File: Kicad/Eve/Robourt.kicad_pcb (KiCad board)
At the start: 4 copper layers, 141.8 x 126 mm, 122 parts, among them IC1 STM32U535RET6, J1 Conn_ST_STDC14, J10 Conn_01x04, J2 Conn_01x02, J3 Conn_02x20_Odd_Even, J4 Conn_01x03, J5 Conn_01x03, J8 Conn_01x04, J9 Conn_01x04, Q1 SQJ504EP-T1_GE3, Q10 SQJ504EP-T1_GE3, Q11 SQJ504EP-T1_GE3, Q12 SQJ504EP-T1_GE3, Q2 SQJ504EP-T1_GE3, Q3 SQJ504EP-T1_GE3, Q4 SQJ504EP-T1_GE3, Q5 SQJ504EP-T1_GE3, Q6 SQJ504EP-T1_GE3, Q7 SQJ504EP-T1_GE3, Q8 SQJ504EP-T1_GE3, Q9 SQJ504EP-T1_GE3, SW2 SW_Push, U1 BU33SD5WG-TR, U3 TMC2590-TA, U4 TMC2590-TA, U5 TMC2590-TA, Y2 Crystal

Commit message: pulled last changes from charlotte
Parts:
- moved R4 9.03 mm to (122.7, 121.2)
- moved C7 9.03 mm to (119.7, 124.8)
- moved D3 9.03 mm to (125.0, 121.2)
- moved U1 9.03 mm to (123.7, 125.9)
- moved C6 9.03 mm to (119.7, 127.0)
- moved R20 2.36 mm to (81.2, 129.8)
- moved R23 1.60 mm to (93.8, 133.9)
- moved R28 1.32 mm to (69.7, 90.3)
- moved R22 1.31 mm to (83.0, 133.9)
- moved C21 0.81 mm to (87.9, 118.5)
- moved R8 0.74 mm to (95.0, 128.2)
- moved R31 0.64 mm to (81.0, 94.3)
- moved C47 0.51 mm to (75.8, 80.4)
- moved R30 0.37 mm to (71.6, 94.2)
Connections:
- U4 pad 26: /driver_stepper1/STANDALONE_MODE -> (no net)
- U4 pad 27: /driver_stepper1/SG_TST -> (no net)
- U5 pad 26: /driver_stepper2/STANDALONE_MODE -> (no net)
- U5 pad 27: /driver_stepper2/SG_TST -> (no net)
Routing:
- net SPI2_MISO: track 0.00 -> 106.4 mm, vias 0 -> 3
- net SPI2_MOSI: track 0.00 -> 106.4 mm, vias 0 -> 3
- net /driver_stepper2/B1: track 2.23 -> 77.9 mm, vias 0 -> 2
- net /driver_stepper2/B2: track 2.23 -> 75.6 mm, vias 0 -> 2
- net GPIO_STEP3: track 0.00 -> 61.1 mm, vias 0 -> 2
- net /driver_stepper/B1: track 2.23 -> 62.0 mm
- net GPIO_DIR3: track 0.00 -> 59.2 mm, vias 0 -> 2
- net 24V: track 0.00 -> 58.0 mm, vias 0 -> 14
- net GPIO_CSN3: track 0.00 -> 53.7 mm, vias 0 -> 2
- net /driver_stepper/B2: track 2.23 -> 55.2 mm
- net /driver_stepper2/5VOUT: track 0.00 -> 50.0 mm, vias 0 -> 2
- net SCK: track 0.00 -> 48.2 mm, vias 0 -> 2
- net /driver_stepper2/VHS: track 0.00 -> 47.6 mm, vias 0 -> 2
- net UART4_TX: track 0.00 -> 37.6 mm, vias 0 -> 2
- net /driver_stepper/5VOUT: track 0.00 -> 37.4 mm, vias 0 -> 2
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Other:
- board text added: "EVE"

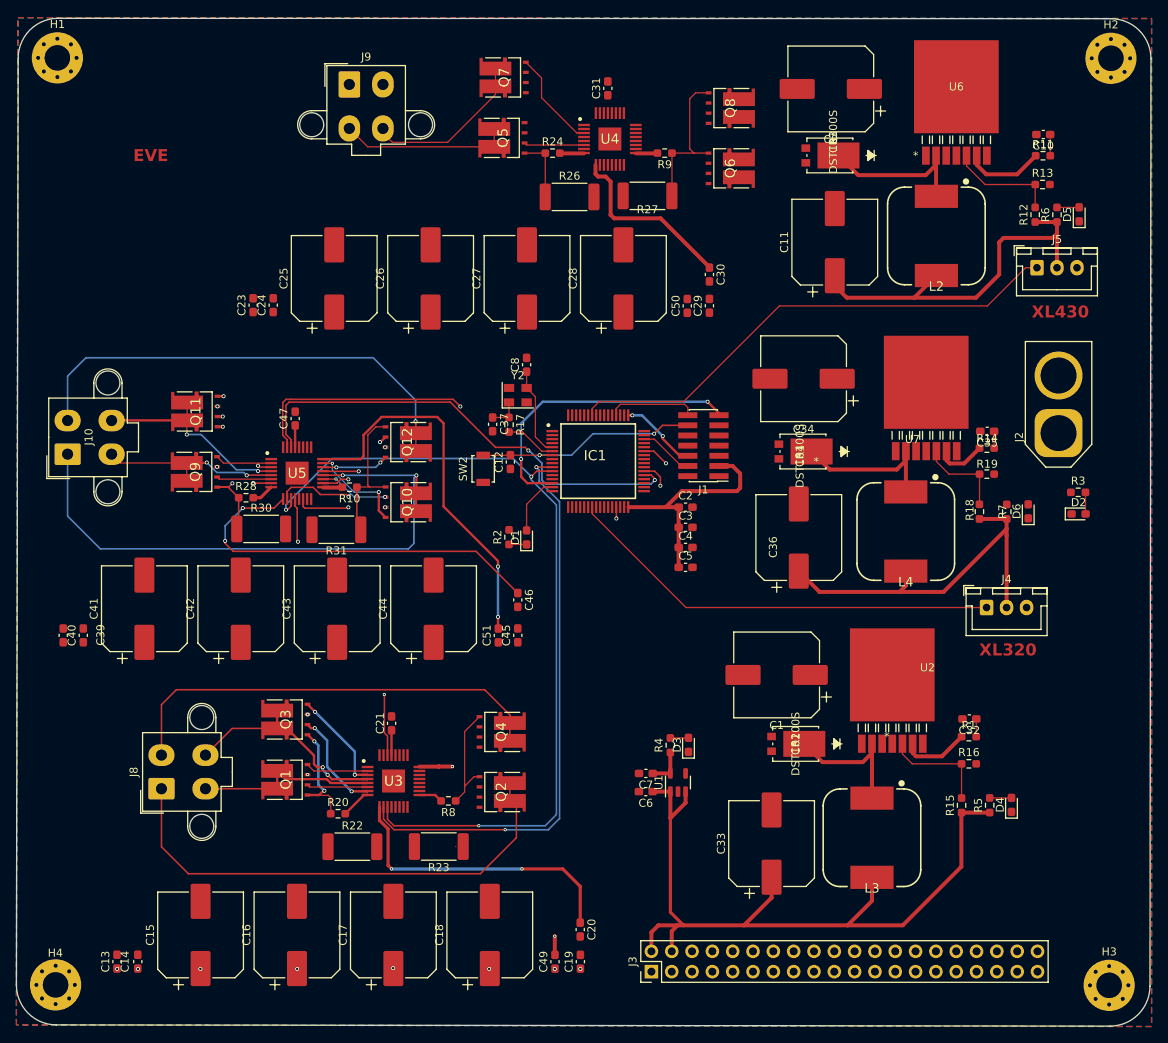
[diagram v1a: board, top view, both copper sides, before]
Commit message: finished routing errors remain
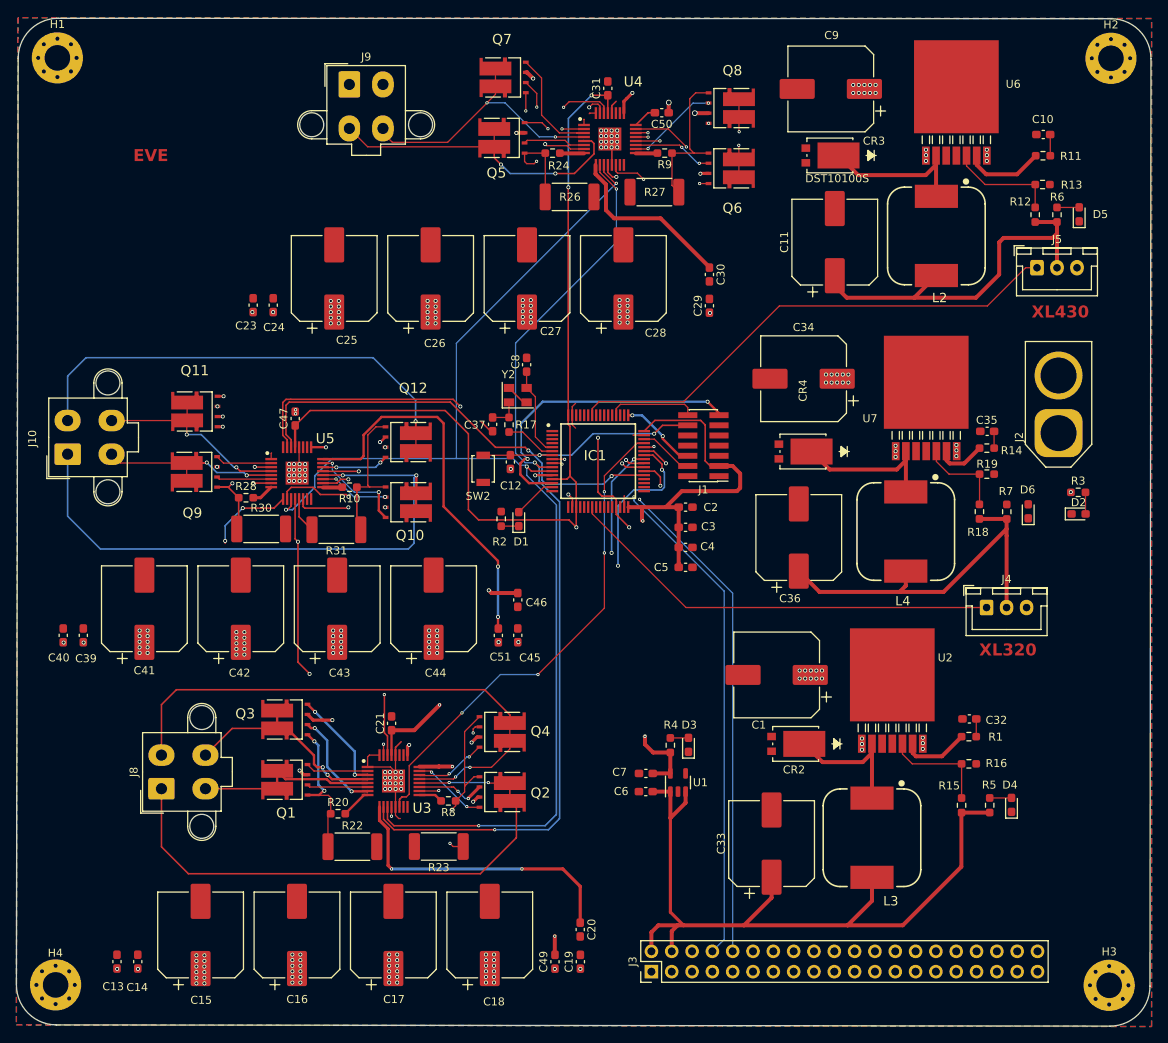
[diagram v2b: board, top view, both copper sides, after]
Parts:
- moved C50 24.4 mm to (121.7, 42.2), turned to 180 degrees
- moved D1 2.49 mm to (103.8, 93.0)
- moved R2 2.49 mm to (101.6, 92.9)
- moved R27 0.98 mm to (120.8, 52.1)
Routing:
- net +3.3V: track 39.6 -> 242.4 mm, vias 0 -> 6
- net SCK: track 48.2 -> 137.6 mm, vias 2 -> 6
- net LPUART1_TX: track 0.00 -> 75.9 mm, vias 0 -> 2
- net LPUART1_RX: track 0.00 -> 74.9 mm, vias 0 -> 2
- net GPIO_CSN1: track 0.00 -> 61.7 mm, vias 0 -> 4
- net GPIO_STEP1: track 0.00 -> 60.0 mm, vias 0 -> 3
- net GPIO_DIR2: track 0.00 -> 59.5 mm, vias 0 -> 2
- net /driver_stepper1/B1: track 0.00 -> 58.9 mm, vias 0 -> 2
- net /driver_stepper1/B2: track 0.00 -> 54.7 mm, vias 0 -> 2
- net GPIO_STEP2: track 0.00 -> 52.7 mm, vias 0 -> 2
- net GPIO_DIR1: track 7.73 -> 57.6 mm, vias 1 -> 3
- net SPI2_MOSI: track 106.4 -> 153.5 mm, vias 3 -> 4
- net SPI2_MISO: track 106.4 -> 152.8 mm, vias 3 -> 4
- net GND: track 0.00 -> 44.3 mm, vias 0 -> 53
- net GPIO_CSN2: track 0.00 -> 39.9 mm, vias 0 -> 2
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
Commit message: started cleaning PCB
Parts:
- moved C14 73.4 mm to (119.4, 111.0)
- moved C13 73.4 mm to (116.8, 111.0)
- moved C39 58.7 mm to (105.6, 107.1)
- moved C40 58.7 mm to (108.1, 107.1)
- moved Q3 14.2 mm to (62.7, 120.1)
- moved Q1 14.1 mm to (62.7, 127.4)
- moved J8 13.0 mm to (46.1, 127.2)
- moved R22 10.1 mm to (73.1, 131.7)
- moved Q4 9.55 mm to (109.1, 118.7), turned to 90 degrees
- moved C15 6.88 mm to (57.1, 145.2)
- moved C16 6.88 mm to (69.2, 145.2)
- moved C17 6.88 mm to (81.2, 145.2)
- moved C18 6.88 mm to (93.3, 145.2)
- moved R8 1.51 mm to (94.8, 129.7)
- moved C42 0.15 mm to (69.2, 104.2)
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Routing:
- net /driver_stepper/B2: track 69.1 -> 6.79 mm
- net /driver_stepper/B1: track 73.4 -> 13.6 mm
- net /driver_stepper/A1: track 23.1 -> 0.00 mm
- net /driver_stepper/A2: track 27.4 -> 10.8 mm, vias 2 -> 1
- net Net-(Q1-S1): track 18.2 -> 10.4 mm, vias 2 -> 0
- net 24V: track 19.4 -> 13.4 mm, vias 204 -> 201
- net /driver_stepper/HA1: track 7.85 -> 2.20 mm
- net /driver_stepper/HB1: track 9.39 -> 13.7 mm
- net /driver_stepper/LB2: track 12.9 -> 16.7 mm, vias 2 -> 3
- net GPIO_DIR1: track 57.6 -> 54.4 mm
- net /driver_stepper/SRB: track 3.02 -> 4.48 mm
- net /driver_stepper/HA2: track 12.9 -> 11.4 mm, vias 2 -> 1
- net GND: track 44.3 -> 42.9 mm
- net +3.3V: track 242.4 -> 241.3 mm
- net Net-(Q2-S1): track 21.7 -> 22.4 mm, vias 2 -> 1
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
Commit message: EVE 2.0 WIP
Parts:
- removed C15, C16, C17, C18, C25, C26: 150u, Capacitor_SMD:CP_Elec_10x10.5
- moved J2 117.2 mm to (74.4, 148.2), turned to 180 degrees
- moved C13 77.6 mm to (72.0, 47.5), turned to 180 degrees
- moved Q6 66.7 mm to (61.8, 55.4), turned to 90 degrees
- moved Q8 63.0 mm to (68.5, 61.8), turned to 180 degrees
- moved C30 61.9 mm to (65.8, 58.1), turned to 180 degrees
- moved C41 56.8 mm to (87.6, 56.2), turned to 0 degrees
- moved Reset 56.5 mm to (123.8, 35.8)
- moved C12 56.0 mm to (128.3, 36.0)
- moved C14 53.2 mm to (75.6, 80.8), turned to 0 degrees
- moved J1 50.8 mm to (109.9, 35.9), turned to -90 degrees
- moved R9 48.8 mm to (75.0, 60.4), turned to 0 degrees
- moved C45 47.5 mm to (87.9, 62.8), turned to 0 degrees
- moved R2 46.6 mm to (121.0, 50.5), turned to -90 degrees
- moved D1 46.5 mm to (122.8, 50.5), turned to -90 degrees
- moved C20 45.4 mm to (68.5, 129.7), turned to 180 degrees
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- renumbered SW2 to Reset
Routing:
- net 5.1V: track 96.8 -> 37.5 mm, vias 0 -> 47
- net /driver_stepper/B2: track 6.79 -> 64.9 mm
- net GND: track 42.9 -> 99.0 mm
- net UART4_RX: track 11.1 -> 66.0 mm, vias 0 -> 2
- net /NRST: track 28.7 -> 79.2 mm
- net /SYS_JTMS-SWDIO: track 6.85 -> 55.5 mm, vias 0 -> 2
- net /SYS_JTMS-SWCLK: track 9.75 -> 58.0 mm
- net /driver_stepper2/5VOUT: track 49.8 -> 4.20 mm, vias 3 -> 0
- net /driver_stepper2/VHS: track 47.6 -> 4.47 mm, vias 2 -> 0
- net 7.5V: track 47.7 -> 4.94 mm, vias 0 -> 47
- net +3.3V: track 241.3 -> 281.9 mm, vias 6 -> 12
- net /driver_stepper/B1: track 13.6 -> 52.0 mm
- net /driver_stepper2/B1: track 77.8 -> 43.8 mm
- net /driver_stepper/5VOUT: track 37.4 -> 5.12 mm, vias 2 -> 0
- net /driver_stepper/VHS: track 33.6 -> 2.90 mm, vias 2 -> 0
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- added copper zone on In2.Cu, net +3.3V
- added copper zone on In2.Cu, net 5.1V
- added copper zone on In2.Cu, net 7.5V

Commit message: update pcb
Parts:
- removed C12, C13, C14, C19, C21, C23, C24, C29, C31, C39, C40, C45, C47: 100n, Capacitor_SMD:C_0603_1608Metric_Pad1.08x0.95mm_HandSolder
- removed C20, C30, C46: 470n, Capacitor_SMD:C_0603_1608Metric_Pad1.08x0.95mm_HandSolder
- removed C27, C28, C41, C42, C43, C44: 150u, Capacitor_SMD:CP_Elec_10x10.5
- removed C37, C8: 10p, Capacitor_SMD:C_0603_1608Metric_Pad1.08x0.95mm_HandSolder
- removed C49, C50, C51: 220n, Capacitor_SMD:C_0603_1608Metric_Pad1.08x0.95mm_HandSolder
- removed C6, C7: 1u, Capacitor_SMD:C_0603_1608Metric_Pad1.08x0.95mm_HandSolder
- removed D3: LED, LED_SMD:LED_0603_1608Metric_Pad1.05x0.95mm_HandSolder
- removed J10, J8, J9: Conn_01x04, Connector_Molex:Molex_Mini-Fit_Jr_5566-04A2_2x02_P4.20mm_Vertical
- removed Q1, Q10, Q11, Q12, Q2, Q3, Q4, Q5, Q6, Q7, Q8, Q9: SQJ504EP-T1_GE3, Mosfet:SQJ968EPT1GE3
- removed R10, R20, R24, R28, R8, R9: 10, Resistor_SMD:R_0603_1608Metric_Pad0.98x0.95mm_HandSolder
- removed R17: 10R, Resistor_SMD:R_0603_1608Metric_Pad0.98x0.95mm_HandSolder
- removed R22, R23, R26, R27, R30, R31: 0.075, Resistor_SMD:R_2512_6332Metric_Pad1.40x3.35mm_HandSolder
- removed R4: 1k, Resistor_SMD:R_0603_1608Metric_Pad0.98x0.95mm_HandSolder
- removed Reset: SW_Push, Button_Switch_SMD:SW_SPST_B3U-1000P
- removed U1: BU33SD5WG-TR, Package_TO_SOT_SMD:SOT-23-5
- removed U3, U4, U5: TMC2590-TA, TMC2590:QFP50P700X700X114-33N
- removed Y2: Crystal, Crystal:Crystal_SMD_EuroQuartz_MT-4Pin_3.2x2.5mm
- added C103: 100n, Capacitor_SMD:C_0402_1005Metric, F.Cu at (307.2, -139.6)
- added C104: 100n, Capacitor_SMD:C_0402_1005Metric, F.Cu at (307.2, -137.6)
- added C107: 100n, Capacitor_SMD:C_0402_1005Metric, F.Cu at (377.5, -135.3)
- added C108: 100n, Capacitor_SMD:C_0402_1005Metric, F.Cu at (377.5, -130.3)
- added C109: 100n, Capacitor_SMD:C_0402_1005Metric, F.Cu at (307.2, -135.7)
- added C110: 100n, Capacitor_SMD:C_0402_1005Metric, F.Cu at (307.2, -133.7)
- added C111: 4.7u, Capacitor_SMD:C_0402_1005Metric, F.Cu at (377.5, -132.8)
- added C112: 100n, Capacitor_SMD:C_0402_1005Metric, F.Cu at (13.2, -114.3)
- added C113: 100n, Capacitor_SMD:C_0402_1005Metric, F.Cu at (13.2, -112.3)
- added C114: 100n, Capacitor_SMD:C_0402_1005Metric, F.Cu at (13.2, -110.4)
- added C115: 100n, Capacitor_SMD:C_0402_1005Metric, F.Cu at (13.2, -108.4)
- added C116: 10p, Capacitor_SMD:C_0402_1005Metric, F.Cu at (45.0, -25.0)
- added C117: 10p, Capacitor_SMD:C_0402_1005Metric, F.Cu at (45.0, -22.5)
- added C118: 100n, Capacitor_SMD:C_0402_1005Metric, F.Cu at (16.1, -114.3)
- added C119: 100n, Capacitor_SMD:C_0402_1005Metric, F.Cu at (16.1, -112.3)
- added C120: 100n, Capacitor_SMD:C_0402_1005Metric, F.Cu at (16.1, -110.4)
- added C121: 100n, Capacitor_SMD:C_0402_1005Metric, F.Cu at (16.1, -108.4)
- added C201: 100n, Capacitor_SMD:C_0402_1005Metric, F.Cu at (-12.3, -36.1)
- added C202: 100n, Capacitor_SMD:C_0402_1005Metric, F.Cu at (-12.3, -37.1)
- added C203: 10u, Capacitor_SMD:C_2220_5750Metric, B.Cu at (-9.61, -29.9)
- added C204: 150u, Capacitor_SMD:CP_Elec_10x10.5, F.Cu at (-9.61, -43.3)
- added C205: 150u, Capacitor_SMD:CP_Elec_10x10.5, F.Cu at (-9.61, -29.9)
- added C206: 220n, Capacitor_SMD:C_0402_1005Metric, F.Cu at (3.57, -41.7)
- added C207: 100n, Capacitor_SMD:C_0402_1005Metric, F.Cu at (3.27, -38.1)
- added C208: 470n, Capacitor_SMD:C_0402_1005Metric, F.Cu at (3.27, -35.6)
- added C209: 100n, Capacitor_SMD:C_0402_1005Metric, F.Cu at (3.27, -33.1)
- added C301: 100n, Capacitor_SMD:C_0402_1005Metric, F.Cu at (-106.0, 4.65)
- added C302: 100n, Capacitor_SMD:C_0402_1005Metric, F.Cu at (-106.0, 6.62)
- added C303: 10u, Capacitor_SMD:C_2220_5750Metric, F.Cu at (-100.3, 7.14)
- added C304: 150u, Capacitor_SMD:CP_Elec_10x10.5, F.Cu at (-126.3, 9.69)
- added C305: 150u, Capacitor_SMD:CP_Elec_10x10.5, F.Cu at (-126.3, 21.7)
- added C306: 220n, Capacitor_SMD:C_0402_1005Metric, F.Cu at (-106.0, 8.59)
- added C307: 100n, Capacitor_SMD:C_0402_1005Metric, F.Cu at (-106.0, 10.6)
- added C308: 470n, Capacitor_SMD:C_0402_1005Metric, F.Cu at (-106.0, 12.5)
- added C309: 100n, Capacitor_SMD:C_0402_1005Metric, F.Cu at (-106.0, 14.5)
- added C401: 100n, Capacitor_SMD:C_0402_1005Metric, F.Cu at (-129.6, 78.8)
- added C402: 100n, Capacitor_SMD:C_0402_1005Metric, F.Cu at (-129.6, 80.8)
- added C403: 10u, Capacitor_SMD:C_2220_5750Metric, F.Cu at (-123.9, 81.3)
- added C404: 150u, Capacitor_SMD:CP_Elec_10x10.5, F.Cu at (-149.9, 83.8)
- added C405: 150u, Capacitor_SMD:CP_Elec_10x10.5, F.Cu at (-149.9, 95.9)
- added C406: 220n, Capacitor_SMD:C_0402_1005Metric, F.Cu at (-129.6, 82.7)
- added C407: 100n, Capacitor_SMD:C_0402_1005Metric, F.Cu at (-129.6, 84.7)
- added C408: 470n, Capacitor_SMD:C_0402_1005Metric, F.Cu at (-129.6, 86.7)
- added C409: 100n, Capacitor_SMD:C_0402_1005Metric, F.Cu at (-129.6, 88.6)
- added C501: 1u, Capacitor_SMD:C_0402_1005Metric, F.Cu at (229.1, 109.2)
- added C502: 1u, Capacitor_SMD:C_0402_1005Metric, F.Cu at (229.1, 111.7)
- added D102: LED, LED_SMD:LED_0603_1608Metric, F.Cu at (381.9, -135.3)
- added D103: LED, LED_SMD:LED_0603_1608Metric, F.Cu at (381.9, -132.7)
- added D104: LED, LED_SMD:LED_0603_1608Metric, F.Cu at (381.9, -130.1)
- added D501: LED, LED_SMD:LED_0603_1608Metric, F.Cu at (233.5, 113.7)
- added J102: Conn_01x02, Connector_JST:JST_XH_B2B-XH-A_1x02_P2.50mm_Vertical, F.Cu at (-38.1, 37.9)
- added J103: Conn_01x02, Connector_JST:JST_XH_B2B-XH-A_1x02_P2.50mm_Vertical, F.Cu at (-38.1, 45.7)
- added J104: Conn_01x02, Connector_JST:JST_XH_B2B-XH-A_1x02_P2.50mm_Vertical, F.Cu at (-12.4, -96.3)
- added J105: Conn_01x02, Connector_JST:JST_XH_B2B-XH-A_1x02_P2.50mm_Vertical, F.Cu at (-12.4, -88.5)
- added J106: Conn_01x02, Connector_JST:JST_XH_B2B-XH-A_1x02_P2.50mm_Vertical, F.Cu at (-12.4, -80.7)
- added J107: Conn_01x02, Connector_JST:JST_XH_B2B-XH-A_1x02_P2.50mm_Vertical, F.Cu at (-2.95, -111.9)
- added J111: Conn_01x02, Connector_JST:JST_XH_B2B-XH-A_1x02_P2.50mm_Vertical, F.Cu at (-2.95, -104.1)
- added J112: Conn_01x02, Connector_JST:JST_XH_B2B-XH-A_1x02_P2.50mm_Vertical, F.Cu at (-2.95, -96.3)
- added J113: Conn_01x02, Connector_JST:JST_XH_B2B-XH-A_1x02_P2.50mm_Vertical, F.Cu at (-2.95, -88.5)
- added J114: Conn_01x02, Connector_JST:JST_XH_B2B-XH-A_1x02_P2.50mm_Vertical, F.Cu at (-2.95, -80.7)
- added J201: Conn_01x04, Connector_Molex:Molex_Mini-Fit_Jr_5566-04A_2x02_P4.20mm_Vertical, F.Cu at (-18.9, -33.9)
- added J301: Conn_01x04, Connector_Molex:Molex_Mini-Fit_Jr_5566-04A_2x02_P4.20mm_Vertical, F.Cu at (-115.4, 6.94)
- added J401: Conn_01x04, Connector_Molex:Molex_Mini-Fit_Jr_5566-04A_2x02_P4.20mm_Vertical, F.Cu at (-139.0, 81.1)
- added Q101: NMOS, Package_TO_SOT_SMD:SOT-23, F.Cu at (-29.5, 42.2)
- added Q201: SQJ504EP-T1_GE3, Mosfet:SQJ968EPT1GE3, F.Cu at (-18.2, -48.8)
- added Q202: SQJ504EP-T1_GE3, Mosfet:SQJ968EPT1GE3, F.Cu at (-18.1, -25.6)
- added Q203: SQJ504EP-T1_GE3, Mosfet:SQJ968EPT1GE3, F.Cu at (-24.0, -48.8)
- added Q204: SQJ504EP-T1_GE3, Mosfet:SQJ968EPT1GE3, F.Cu at (-23.9, -25.6)
- added Q301: SQJ504EP-T1_GE3, Mosfet:SQJ968EPT1GE3, F.Cu at (-129.6, 1.10)
- added Q302: SQJ504EP-T1_GE3, Mosfet:SQJ968EPT1GE3, F.Cu at (-121.5, 1.10)
- added Q303: SQJ504EP-T1_GE3, Mosfet:SQJ968EPT1GE3, F.Cu at (-113.4, 1.10)
- added Q304: SQJ504EP-T1_GE3, Mosfet:SQJ968EPT1GE3, F.Cu at (-105.3, 1.10)
- added Q401: SQJ504EP-T1_GE3, Mosfet:SQJ968EPT1GE3, F.Cu at (-153.2, 75.2)
- added Q402: SQJ504EP-T1_GE3, Mosfet:SQJ968EPT1GE3, F.Cu at (-145.1, 75.2)
- added Q403: SQJ504EP-T1_GE3, Mosfet:SQJ968EPT1GE3, F.Cu at (-137.0, 75.2)
- added Q404: SQJ504EP-T1_GE3, Mosfet:SQJ968EPT1GE3, F.Cu at (-128.9, 75.2)
- added R101: 100k, Resistor_SMD:R_0402_1005Metric, F.Cu at (301.4, -122.2)
- added R102: 100k, Resistor_SMD:R_0402_1005Metric, F.Cu at (301.4, -120.2)
- added R103: 1k, Resistor_SMD:R_0402_1005Metric, F.Cu at (301.4, -118.2)
- added R104: 1k, Resistor_SMD:R_0402_1005Metric, F.Cu at (301.4, -116.2)
- added R106: 390, Resistor_SMD:R_0402_1005Metric, F.Cu at (377.5, -122.8)
- added R107: 22, Resistor_SMD:R_0402_1005Metric, F.Cu at (-30.0, 48.3)
- added R108: 10k, Resistor_SMD:R_0402_1005Metric, F.Cu at (-30.0, 50.2)
- added R109: 390, Resistor_SMD:R_0402_1005Metric, F.Cu at (377.5, -120.3)
- added R110: 100k, Resistor_SMD:R_0402_1005Metric, F.Cu at (301.4, -110.2)
- added R111: 100k, Resistor_SMD:R_0402_1005Metric, F.Cu at (304.3, -122.2)
- added R112: 1k, Resistor_SMD:R_0402_1005Metric, F.Cu at (304.3, -120.2)
- added R113: 1k, Resistor_SMD:R_0402_1005Metric, F.Cu at (304.3, -118.2)
- added R114: 390, Resistor_SMD:R_0402_1005Metric, F.Cu at (377.5, -117.8)
- added R115: 100k, Resistor_SMD:R_0402_1005Metric, F.Cu at (7.39, -90.9)
- added R116: 100k, Resistor_SMD:R_0402_1005Metric, F.Cu at (7.39, -88.9)
- added R117: 100k, Resistor_SMD:R_0402_1005Metric, F.Cu at (7.39, -86.9)
- added R118: 100k, Resistor_SMD:R_0402_1005Metric, F.Cu at (7.39, -85.0)
- added R120: 1k, Resistor_SMD:R_0402_1005Metric, F.Cu at (10.3, -96.9)
- added R121: 1k, Resistor_SMD:R_0402_1005Metric, F.Cu at (10.3, -94.9)
- added R122: 1k, Resistor_SMD:R_0402_1005Metric, F.Cu at (10.3, -92.9)
- added R123: 1k, Resistor_SMD:R_0402_1005Metric, F.Cu at (10.3, -90.9)
- added R124: 10R, Resistor_SMD:R_0402_1005Metric, F.Cu at (45.0, -12.4)
- added R125: 100k, Resistor_SMD:R_0402_1005Metric, F.Cu at (10.3, -88.9)
- added R126: 100k, Resistor_SMD:R_0402_1005Metric, F.Cu at (10.3, -86.9)
- added R127: 100k, Resistor_SMD:R_0402_1005Metric, F.Cu at (10.3, -85.0)
- added R128: 100k, Resistor_SMD:R_0402_1005Metric, F.Cu at (13.2, -96.9)
- added R129: 1k, Resistor_SMD:R_0402_1005Metric, F.Cu at (13.2, -94.9)
- added R130: 1k, Resistor_SMD:R_0402_1005Metric, F.Cu at (13.2, -92.9)
- added R131: 1k, Resistor_SMD:R_0402_1005Metric, F.Cu at (13.2, -90.9)
- added R132: 1k, Resistor_SMD:R_0402_1005Metric, F.Cu at (13.2, -88.9)
- added R201: 0.075, Resistor_SMD:R_2512_6332Metric, B.Cu at (-21.0, -45.7)
- added R202: 0.075, Resistor_SMD:R_2512_6332Metric, B.Cu at (-21.0, -28.6)
- added R203: 10, Resistor_SMD:R_0402_1005Metric, F.Cu at (3.27, -30.6)
- added R204: 10, Resistor_SMD:R_0402_1005Metric, F.Cu at (3.27, -28.1)
- added R301: 0.075, Resistor_SMD:R_2512_6332Metric, F.Cu at (-103.1, 17.9)
- added R302: 0.075, Resistor_SMD:R_2512_6332Metric, F.Cu at (-103.1, 22.8)
- added R303: 10, Resistor_SMD:R_0402_1005Metric, F.Cu at (-103.1, 11.6)
- added R304: 10, Resistor_SMD:R_0402_1005Metric, F.Cu at (-103.1, 13.6)
- added R401: 0.075, Resistor_SMD:R_2512_6332Metric, F.Cu at (-126.7, 92.1)
- added R402: 0.075, Resistor_SMD:R_2512_6332Metric, F.Cu at (-126.7, 97.0)
- added R403: 10, Resistor_SMD:R_0402_1005Metric, F.Cu at (-126.7, 85.7)
- added R404: 10, Resistor_SMD:R_0402_1005Metric, F.Cu at (-126.7, 87.7)
- added R501: 220, Resistor_SMD:R_0402_1005Metric, F.Cu at (229.1, 114.2)
- added SW101: SW_Push, Button_Switch_SMD:SW_SPST_B3U-1000P, F.Cu at (302.9, -138.4)
- added SW102: SW_Push, Button_Switch_SMD:SW_SPST_B3U-1000P, F.Cu at (302.9, -134.1)
- added SW103: SW_Push, Button_Switch_SMD:SW_SPST_B3U-1000P, F.Cu at (302.9, -129.7)
- added SW104: SW_Push, Button_Switch_SMD:SW_SPST_B3U-1000P, F.Cu at (302.9, -125.4)
- added U201: TMC2590-TA, TMC2590:QFP50P700X700X114-33N, B.Cu at (-9.55, -43.4)
- added U301: TMC2590-TA, TMC2590:QFP50P700X700X114-33N, F.Cu at (-114.3, 21.5)
- added U401: TMC2590-TA, TMC2590:QFP50P700X700X114-33N, F.Cu at (-137.9, 95.6)
- added U501: BU33SD5WG-TR, Package_TO_SOT_SMD:SOT-23-5, F.Cu at (233.8, 110.2)
- added Y101: Crystal, Crystal:Crystal_SMD_EuroQuartz_MT-4Pin_3.2x2.5mm, F.Cu at (49.7, -23.8)
- C101: renamed from C2; footprint Capacitor_SMD:C_0603_1608Metric_Pad1.08x0.95mm_HandSolder -> Capacitor_SMD:C_0402_1005Metric
- C102: renamed from C3; footprint Capacitor_SMD:C_0603_1608Metric_Pad1.08x0.95mm_HandSolder -> Capacitor_SMD:C_0402_1005Metric
- C105: renamed from C4; footprint Capacitor_SMD:C_0603_1608Metric_Pad1.08x0.95mm_HandSolder -> Capacitor_SMD:C_0402_1005Metric
- C106: renamed from C5; footprint Capacitor_SMD:C_0603_1608Metric_Pad1.08x0.95mm_HandSolder -> Capacitor_SMD:C_0402_1005Metric
- C602: renamed from C32; footprint Capacitor_SMD:C_0603_1608Metric_Pad1.08x0.95mm_HandSolder -> Capacitor_SMD:C_0402_1005Metric
- C702: renamed from C10; footprint Capacitor_SMD:C_0603_1608Metric_Pad1.08x0.95mm_HandSolder -> Capacitor_SMD:C_0402_1005Metric
- C802: renamed from C35; footprint Capacitor_SMD:C_0603_1608Metric_Pad1.08x0.95mm_HandSolder -> Capacitor_SMD:C_0402_1005Metric
- CR601: renamed from CR2; footprint libs:DST10100S -> DST10100S:DST10100S
- CR701: renamed from CR3; footprint libs:DST10100S -> DST10100S:DST10100S
- CR801: renamed from CR4; footprint libs:DST10100S -> DST10100S:DST10100S
- D101: renamed from D1; footprint LED_SMD:LED_0603_1608Metric_Pad1.05x0.95mm_HandSolder -> LED_SMD:LED_0603_1608Metric
- D105: renamed from D2; footprint LED_SMD:LED_0603_1608Metric_Pad1.05x0.95mm_HandSolder -> LED_SMD:LED_0603_1608Metric
- D601: renamed from D4; footprint LED_SMD:LED_0603_1608Metric_Pad1.05x0.95mm_HandSolder -> LED_SMD:LED_0603_1608Metric
- D701: renamed from D5; footprint LED_SMD:LED_0603_1608Metric_Pad1.05x0.95mm_HandSolder -> LED_SMD:LED_0603_1608Metric
- D801: renamed from D6; footprint LED_SMD:LED_0603_1608Metric_Pad1.05x0.95mm_HandSolder -> LED_SMD:LED_0603_1608Metric
- J115: renamed from J3; footprint Connector_PinHeader_2.54mm:PinHeader_2x20_P2.54mm_Vertical -> Connector_PinSocket_2.54mm:PinSocket_2x20_P2.54mm_Horizontal
- L601: renamed from L3; footprint Eagle_WE-PD (rev23a):WE-PD_1210 -> Inductor_SMD:L_12x12mm_H8mm
- L701: renamed from L2; footprint Eagle_WE-PD (rev23a):WE-PD_1210 -> Inductor_SMD:L_12x12mm_H8mm
- L801: renamed from L4; footprint Eagle_WE-PD (rev23a):WE-PD_1210 -> Inductor_SMD:L_12x12mm_H8mm
- R105: renamed from R2; value 1k -> 390; footprint Resistor_SMD:R_0603_1608Metric_Pad0.98x0.95mm_HandSolder -> Resistor_SMD:R_0402_1005Metric
- R119: renamed from R3; footprint Resistor_SMD:R_0603_1608Metric_Pad0.98x0.95mm_HandSolder -> Resistor_SMD:R_0402_1005Metric
- R601: renamed from R1; footprint Resistor_SMD:R_0603_1608Metric_Pad0.98x0.95mm_HandSolder -> Resistor_SMD:R_0402_1005Metric
- R602: renamed from R15; footprint Resistor_SMD:R_0603_1608Metric_Pad0.98x0.95mm_HandSolder -> Resistor_SMD:R_0402_1005Metric
- R603: renamed from R16; footprint Resistor_SMD:R_0603_1608Metric_Pad0.98x0.95mm_HandSolder -> Resistor_SMD:R_0402_1005Metric
- R604: renamed from R5; footprint Resistor_SMD:R_0603_1608Metric_Pad0.98x0.95mm_HandSolder -> Resistor_SMD:R_0402_1005Metric
- R701: renamed from R11; footprint Resistor_SMD:R_0603_1608Metric_Pad0.98x0.95mm_HandSolder -> Resistor_SMD:R_0402_1005Metric
- R702: renamed from R12; footprint Resistor_SMD:R_0603_1608Metric_Pad0.98x0.95mm_HandSolder -> Resistor_SMD:R_0402_1005Metric
- R703: renamed from R13; footprint Resistor_SMD:R_0603_1608Metric_Pad0.98x0.95mm_HandSolder -> Resistor_SMD:R_0402_1005Metric
- R704: renamed from R6; value 1k -> 680; footprint Resistor_SMD:R_0603_1608Metric_Pad0.98x0.95mm_HandSolder -> Resistor_SMD:R_0402_1005Metric
- R801: renamed from R14; footprint Resistor_SMD:R_0603_1608Metric_Pad0.98x0.95mm_HandSolder -> Resistor_SMD:R_0402_1005Metric
- R802: renamed from R18; footprint Resistor_SMD:R_0603_1608Metric_Pad0.98x0.95mm_HandSolder -> Resistor_SMD:R_0402_1005Metric
- R803: renamed from R19; footprint Resistor_SMD:R_0603_1608Metric_Pad0.98x0.95mm_HandSolder -> Resistor_SMD:R_0402_1005Metric
- R804: renamed from R7; value 1k -> 375; footprint Resistor_SMD:R_0603_1608Metric_Pad0.98x0.95mm_HandSolder -> Resistor_SMD:R_0402_1005Metric
- U601: renamed from U2; value ~ -> LT1076CR-PBF; footprint libs:LT1076CR-PBF -> LT1076CR:LT1076CR-PBF
- U701: renamed from U6; value ~ -> LT1076CR-PBF; footprint libs:LT1076CR-PBF -> LT1076CR:LT1076CR-PBF
- U801: renamed from U7; value ~ -> LT1076CR-PBF; footprint libs:LT1076CR-PBF -> LT1076CR:LT1076CR-PBF
- moved J110 331.2 mm to (403.9, 114.3)
- moved C101 308.5 mm to (338.3, -107.3)
- moved C102 308.5 mm to (338.3, -109.9)
- moved C105 308.5 mm to (338.3, -112.4)
- moved C106 308.5 mm to (338.3, -114.9)
- moved D101 308.5 mm to (345.0, -163.5)
- moved R105 308.5 mm to (343.2, -163.5)
- moved IC101 308.5 mm to (335.9, -128.3)
- moved J101 249.5 mm to (341.6, -56.5)
- moved D105 239.4 mm to (414.7, 145.0)
- moved J108 239.4 mm to (413.7, 137.5)
- moved R119 239.4 mm to (414.6, 142.3)
- moved J109 239.4 mm to (414.0, 99.0)
- moved H102 163.5 mm to (40.0, 63.0)
- moved C601 141.5 mm to (191.3, -18.1)
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- renumbered C1 to C601, C33 to C603, C9 to C701, C11 to C703, C34 to C801, C36 to C803, H4 to H101, H3 to H102, H2 to H103, H1 to H104, IC1 to IC101, J1 to J101, J4 to J108, J5 to J109, J2 to J110
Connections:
- D101 pad 2: /Test_LED -> /USR_LED_1
- IC101 pad 1: unconnected-(IC1-VBAT-Pad1) -> +3.3V
- IC101 pad 10: SPI2_MISO -> unconnected-(IC101-PC2-Pad10)
- IC101 pad 11: SPI2_MOSI -> unconnected-(IC101-PC3-Pad11)
- IC101 pad 15: /Test_LED -> UART4_RX
- IC101 pad 20: unconnected-(IC1-PA4-Pad20) -> /FDC_1
- IC101 pad 21: unconnected-(IC1-PA5-Pad21) -> /FDC_2
- IC101 pad 22: unconnected-(IC1-PA6-Pad22) -> /FDC_3
- IC101 pad 23: USART3_TX -> /FDC_4
- IC101 pad 24: unconnected-(IC1-PC4-Pad24) -> /FDC_5
- IC101 pad 25: unconnected-(IC1-PC5-Pad25) -> /FDC_6
- IC101 pad 26: unconnected-(IC1-PB0-Pad26) -> /FDC_7
- IC101 pad 27: unconnected-(IC1-PB1-Pad27) -> /FDC_8
- IC101 pad 29: SCK -> unconnected-(IC101-PB10-Pad29)
- IC101 pad 30: unconnected-(IC1-VCAP-Pad30) -> /Vcap
- IC101 pad 34: unconnected-(IC1-PB13-Pad34) -> SCK
- IC101 pad 35: unconnected-(IC1-PB14-Pad35) -> SPI2_MISO
- IC101 pad 36: unconnected-(IC1-PB15-Pad36) -> SPI2_MOSI
- IC101 pad 37: GPIO_DIR3 -> GPIO_CSN3
- IC101 pad 38: GPIO_STEP3 -> GPIO_CSN2
- IC101 pad 39: GPIO_DIR2 -> GPIO_CSN1
- IC101 pad 40: GPIO_STEP2 -> unconnected-(IC101-PC9-Pad40)
- IC101 pad 41: GPIO_DIR1 -> /USR_LED_4
- IC101 pad 42: GPIO_STEP1 -> /USR_LED_3
- IC101 pad 43: GPIO_CSN3 -> /USR_LED_2
- IC101 pad 44: GPIO_CSN2 -> /USR_LED_1
- IC101 pad 45: GPIO_CSN1 -> unconnected-(IC101-PA12-Pad45)
- IC101 pad 51: unconnected-(IC1-PC10-Pad51) -> /USR_BTN_3
- IC101 pad 52: UART4_RX -> /USR_BTN_2
- IC101 pad 53: UART5_TX -> /USR_BTN_1
- IC101 pad 55: unconnected-(IC1-PB3-Pad55) -> /SYS_JTDO-SWO
- IC101 pad 60: unconnected-(IC1-PH3-BOOT0-Pad60) -> GND
- IC101 pad 62: unconnected-(IC1-PB9-Pad62) -> /PWM_FAN
- J101 pad 8: unconnected-(J1-JTDO/SWO-Pad8) -> /SYS_JTDO-SWO
- J108 pad 1: USART3_TX -> USART1_TX
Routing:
- net +3.3V: track 281.9 -> 0.00 mm, vias 12 -> 0
- net SPI2_MISO: track 158.4 -> 0.00 mm, vias 4 -> 0
- net SPI2_MOSI: track 149.5 -> 0.00 mm, vias 4 -> 0
- net SCK: track 127.5 -> 0.00 mm, vias 3 -> 0
- net GND: track 99.0 -> 0.00 mm, vias 53 -> 0
- net /NRST: track 79.2 -> 0.00 mm, vias 2 -> 0
- net GPIO_STEP2: track 75.7 -> 0.00 mm, vias 2 -> 0
- net USART1_TX: track 74.7 -> 0.00 mm, vias 1 -> 0
- net USART3_TX: track 73.5 -> 0.00 mm, vias 1 -> 0
- net LPUART1_TX: track 69.6 -> 0.00 mm, vias 1 -> 0
- net LPUART1_RX: track 68.7 -> 0.00 mm, vias 1 -> 0
- net UART4_RX: track 66.0 -> 0.00 mm, vias 2 -> 0
- net /driver_stepper/B2: track 64.9 -> 0.00 mm, vias 2 -> 0
- net UART4_TX: track 61.3 -> 0.00 mm, vias 2 -> 0
- net GPIO_DIR2: track 61.2 -> 0.00 mm, vias 3 -> 0
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- removed copper zone on In2.Cu, net +3.3V
- removed copper zone on In2.Cu, net 24V
- removed copper zone on In2.Cu, net 5.1V
- removed copper zone on In2.Cu, net 7.5V
- removed copper zone on B.Cu, net GND
- removed copper zone on F.Cu, net GND
- removed copper zone on In1.Cu, net GND
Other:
- board size 141.8 x 126 mm -> 85 x 70 mm
- board text removed: "XL320"
- board text removed: "XL430"

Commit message: PCB changes
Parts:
- removed J104, J105, J106, J107, J111, J112, J113, J114: Conn_01x02, Connector_JST:JST_XH_B2B-XH-A_1x02_P2.50mm_Vertical
- added J1: Conn_02x08_Odd_Even, Connector_PinSocket_2.54mm:PinSocket_2x08_P2.54mm_Vertical_SMD, F.Cu at (101.0, 39.4)
- C201, C202, C206, C207, C208, C209, IC101, R203, R204: moved to B.Cu
- moved J108 415.2 mm to (4.50, 67.5)
- moved J109 410.0 mm to (4.50, 79.0)
- moved J110 383.8 mm to (26.0, 46.8), turned to -90 degrees
- moved IC101 320.5 mm to (92.0, 79.5), turned to -90 degrees
- moved D105 287.6 mm to (132.0, 91.7)
- moved R119 287.6 mm to (132.0, 89.0)
- moved D102 276.2 mm to (109.1, -92.5)
- moved D103 275.6 mm to (109.1, -94.2)
- moved D104 275.0 mm to (109.1, -95.8)
- moved R106 272.4 mm to (106.9, -92.4), turned to 90 degrees
- moved R109 271.7 mm to (106.9, -96.4), turned to 90 degrees
- moved R114 271.7 mm to (106.9, -94.4), turned to -90 degrees
- moved J101 265.1 mm to (101.0, 55.0), turned to 0 degrees
- moved C111 263.5 mm to (115.8, -102.4), turned to 90 degrees
- moved C107 254.5 mm to (127.8, -86.6), turned to -90 degrees
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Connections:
- R120 pad 2: Net-(J104-Pin_1) -> unconnected-(R120-Pad2)
- R121 pad 2: Net-(J105-Pin_1) -> unconnected-(R121-Pad2)
- R122 pad 2: Net-(J106-Pin_1) -> unconnected-(R122-Pad2)
- R123 pad 2: Net-(J107-Pin_1) -> unconnected-(R123-Pad2)
- R129 pad 2: Net-(J111-Pin_1) -> unconnected-(R129-Pad2)
- R130 pad 2: Net-(J112-Pin_1) -> unconnected-(R130-Pad2)
- R131 pad 2: Net-(J113-Pin_1) -> unconnected-(R131-Pad2)
- R132 pad 2: Net-(J114-Pin_1) -> unconnected-(R132-Pad2)
- R202 pad 1: Net-(Q202-S2) -> /driver_stepper/S
- R204 pad 1: Net-(Q202-S2) -> /driver_stepper/S
- R302 pad 1: Net-(Q302-S2) -> /driver_stepper1/S
- R304 pad 1: Net-(Q302-S2) -> /driver_stepper1/S
- R402 pad 1: Net-(Q402-S2) -> /driver_stepper2/S
- R404 pad 1: Net-(Q402-S2) -> /driver_stepper2/S
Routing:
- net /driver_stepper/LB1: track 0.00 -> 35.8 mm, vias 0 -> 2
- net /driver_stepper/B2: track 0.00 -> 34.7 mm, vias 0 -> 2
- net /driver_stepper/B1: track 0.00 -> 33.2 mm, vias 0 -> 2
- net /driver_stepper/LB2: track 0.00 -> 32.1 mm, vias 0 -> 2
- net GND: track 0.00 -> 31.9 mm, vias 0 -> 9
- net /driver_stepper/HB2: track 0.00 -> 27.3 mm, vias 0 -> 2
- net /driver_stepper/SRB: track 0.00 -> 22.5 mm, vias 0 -> 2
- net /driver_stepper/A2: track 0.00 -> 20.9 mm, vias 0 -> 2
- net /driver_stepper/HA2: track 0.00 -> 19.4 mm, vias 0 -> 2
- net /driver_stepper/HB1: track 0.00 -> 18.2 mm, vias 0 -> 2
- net /driver_stepper/HA1: track 0.00 -> 15.5 mm, vias 0 -> 2
- net Net-(Q201-S1): track 0.00 -> 14.1 mm, vias 0 -> 2
- net /driver_stepper/LA2: track 0.00 -> 13.2 mm, vias 0 -> 2
- net /driver_stepper/A1: track 0.00 -> 12.2 mm, vias 0 -> 1
- net 24V: track 0.00 -> 11.9 mm, vias 0 -> 10
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- added copper zone on In2.Cu, net 24V
- added copper zone on B.Cu, net GND
- added copper zone on F.Cu, net GND
- added copper zone on In1.Cu, net GND
